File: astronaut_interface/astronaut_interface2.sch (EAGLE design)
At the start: 17 parts, among them IC1 PCF8591T, J1 UI, J2 Display, P1 JT9S-19, U1 TACT-12MM, U2 TACT-12MM, U3 TACT-12MM, U4 TACT-12MM

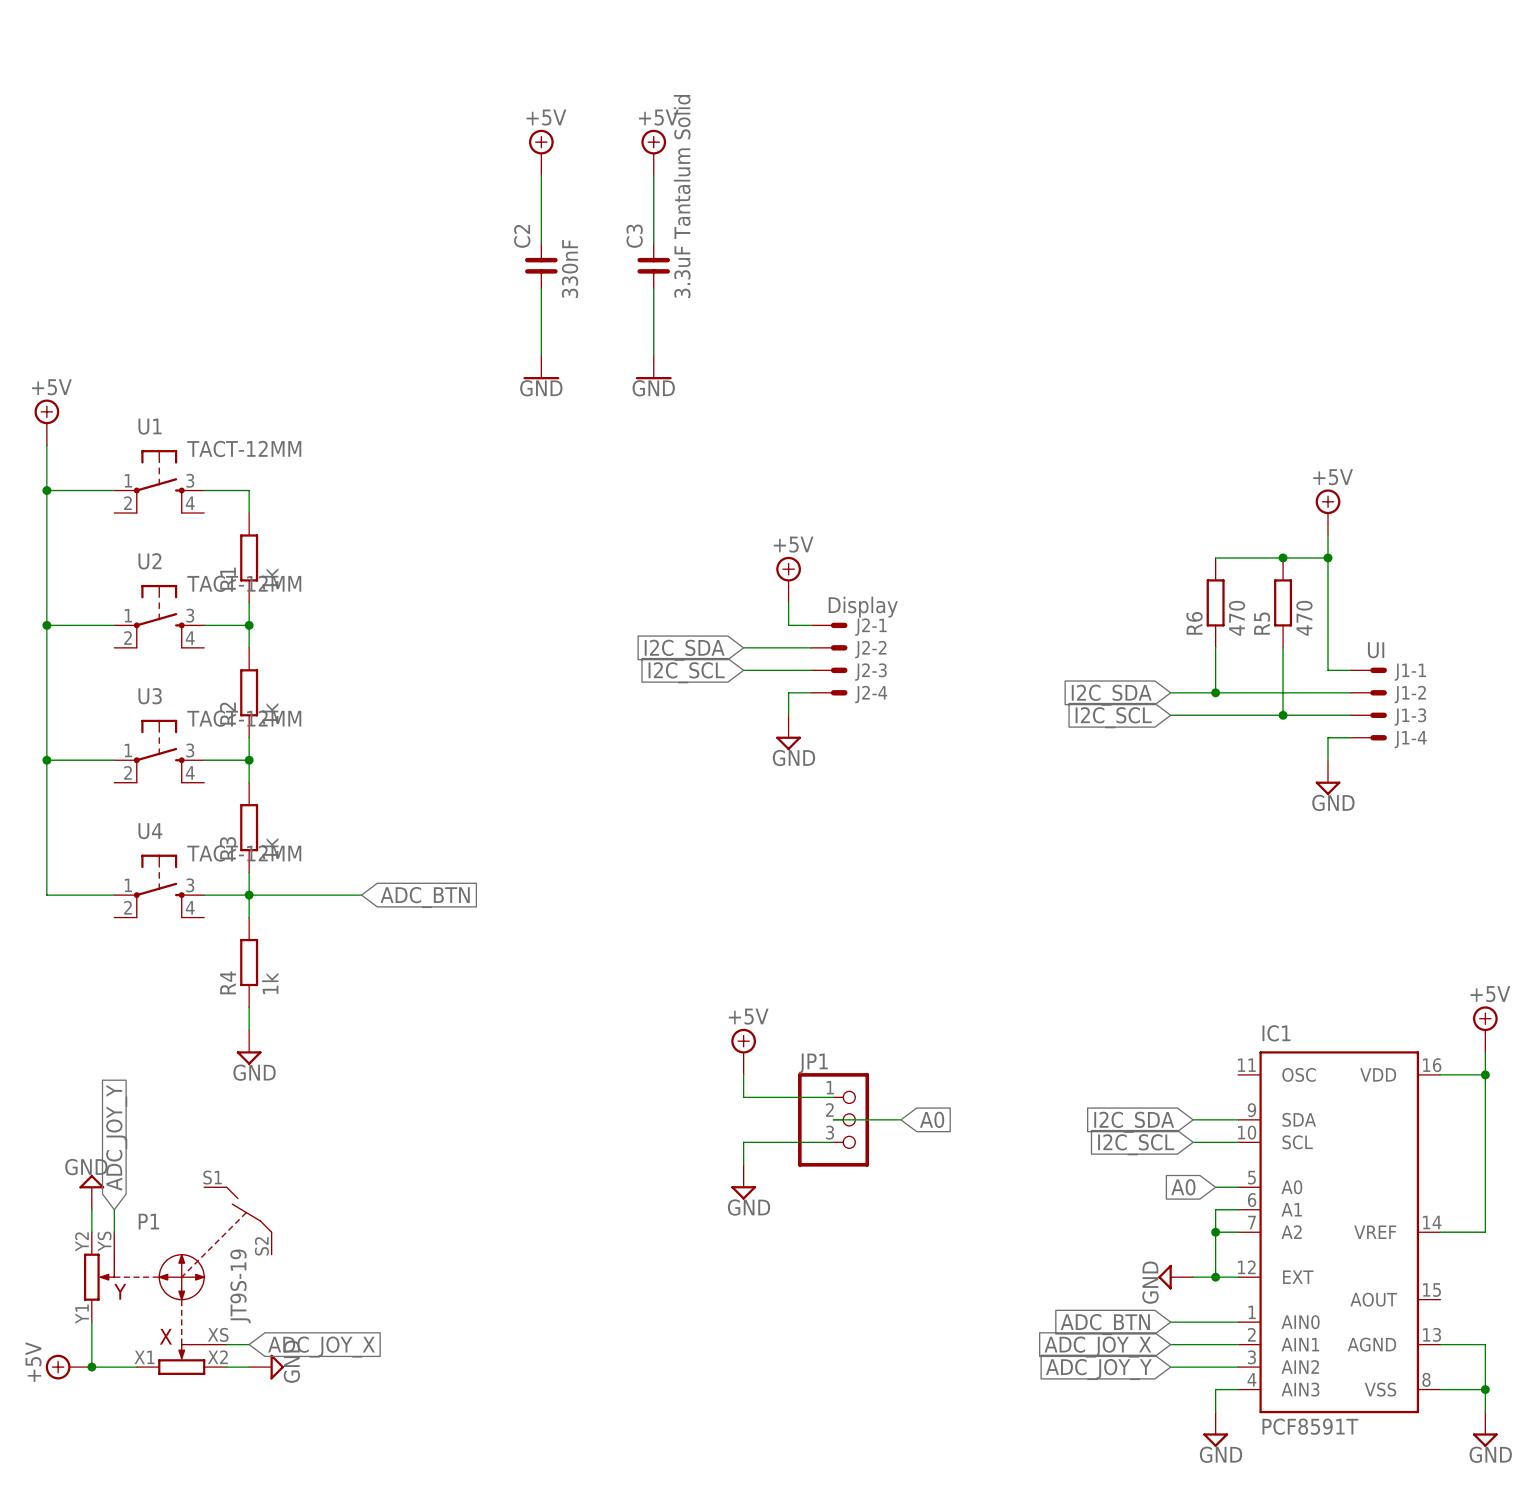
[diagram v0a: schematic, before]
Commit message: corrected gerbers, cleaned schematics, added documnetation
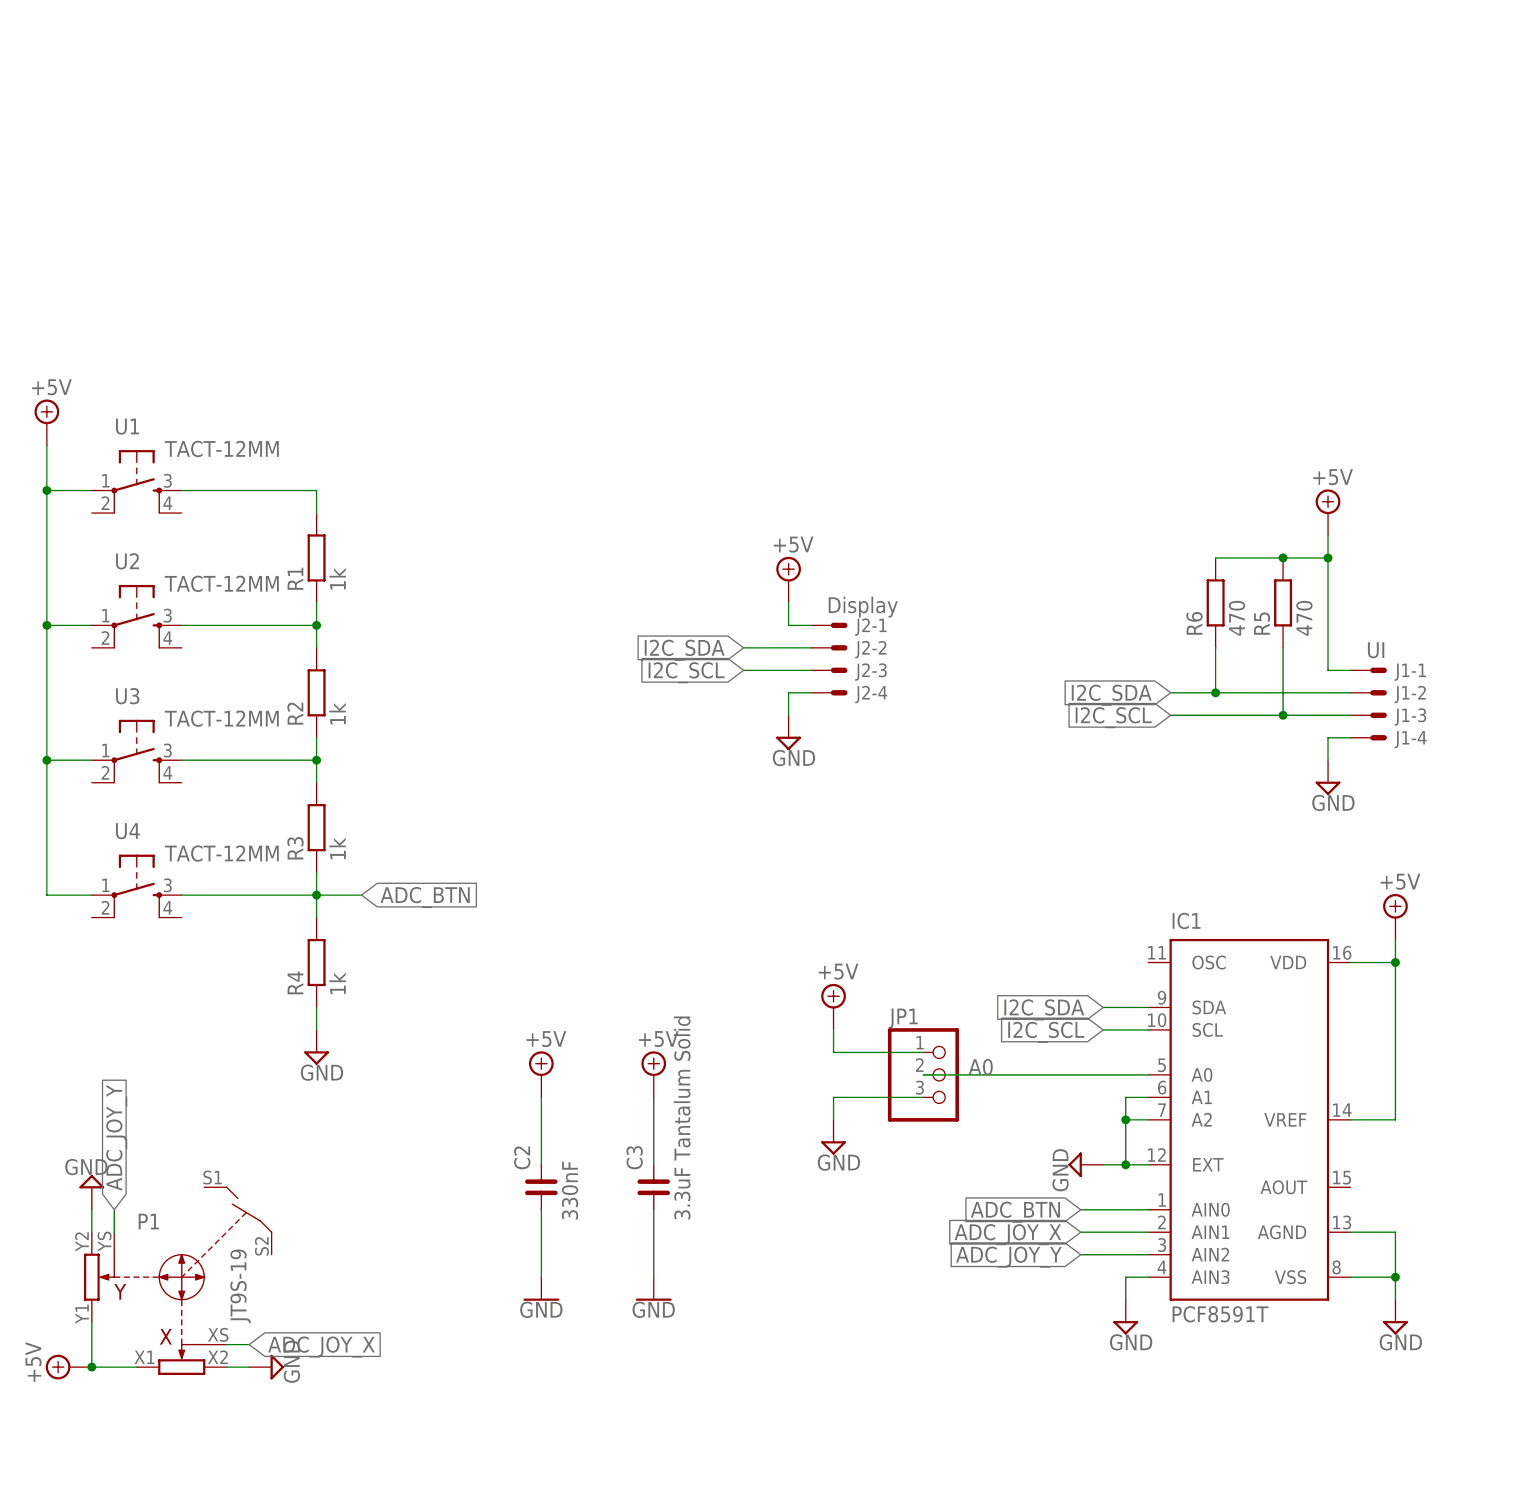
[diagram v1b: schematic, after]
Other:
- moved on the sheet: C2, C3, IC1, JP1, R1, R2, R3, R4, U1, U2, U3, U4
